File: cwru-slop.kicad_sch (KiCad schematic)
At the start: 65 parts, among them J1 USB_C_Receptacle_USB2.0_16P, J2 FTSH-105-01-L-DV-007-K, J3 Conn_01x03_Pin, J4 54-00320, U1 TLV9001IDCK, U10 B3U-1000P, U11 TLV9001IDCK, U12 TLV9001IDCK, U2 AP63205WU, U3 TLV75533PDBV, U4 STM32L433CCTx, U5 TPS2116DRL, U6 FXLS8974CFR3, U7 ESDCAN24-2BLY, U8 MCP2562-E-SN, U9 24lc32at-i/ot, Y1 XRCGB24M000F3M00R0

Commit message: erc, remove vdda filtering (check if nec), clean
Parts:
- removed C6: 10n, Capacitor_SMD:C_0603_1608Metric_Pad1.08x0.95mm_HandSolder, symbol slopp:C
- removed C7, C8: 1u, Capacitor_SMD:C_0603_1608Metric_Pad1.08x0.95mm_HandSolder, symbol slopp:C
- removed FB1: 120R, Package_QFP:LQFP-48_7x7mm_P0.5mm, symbol Device:FerriteBead
- C14: value 1u -> 10u
- C3: value 100n -> 10n
- C4: value 100n -> 1u
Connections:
- net +3.3V is gone; now on net +3V3: C1.1, C2.1, C3.1, C4.1, C5.1, U4.1 (VBAT), U4.24 (VDD), U4.36 (VDDUSB), U4.48 (VDD)
- net +3.3VA is gone; now on net +3V3: U4.9 (VDDA)
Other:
- moved on the sheet: C1, C2, C3, C4, C5

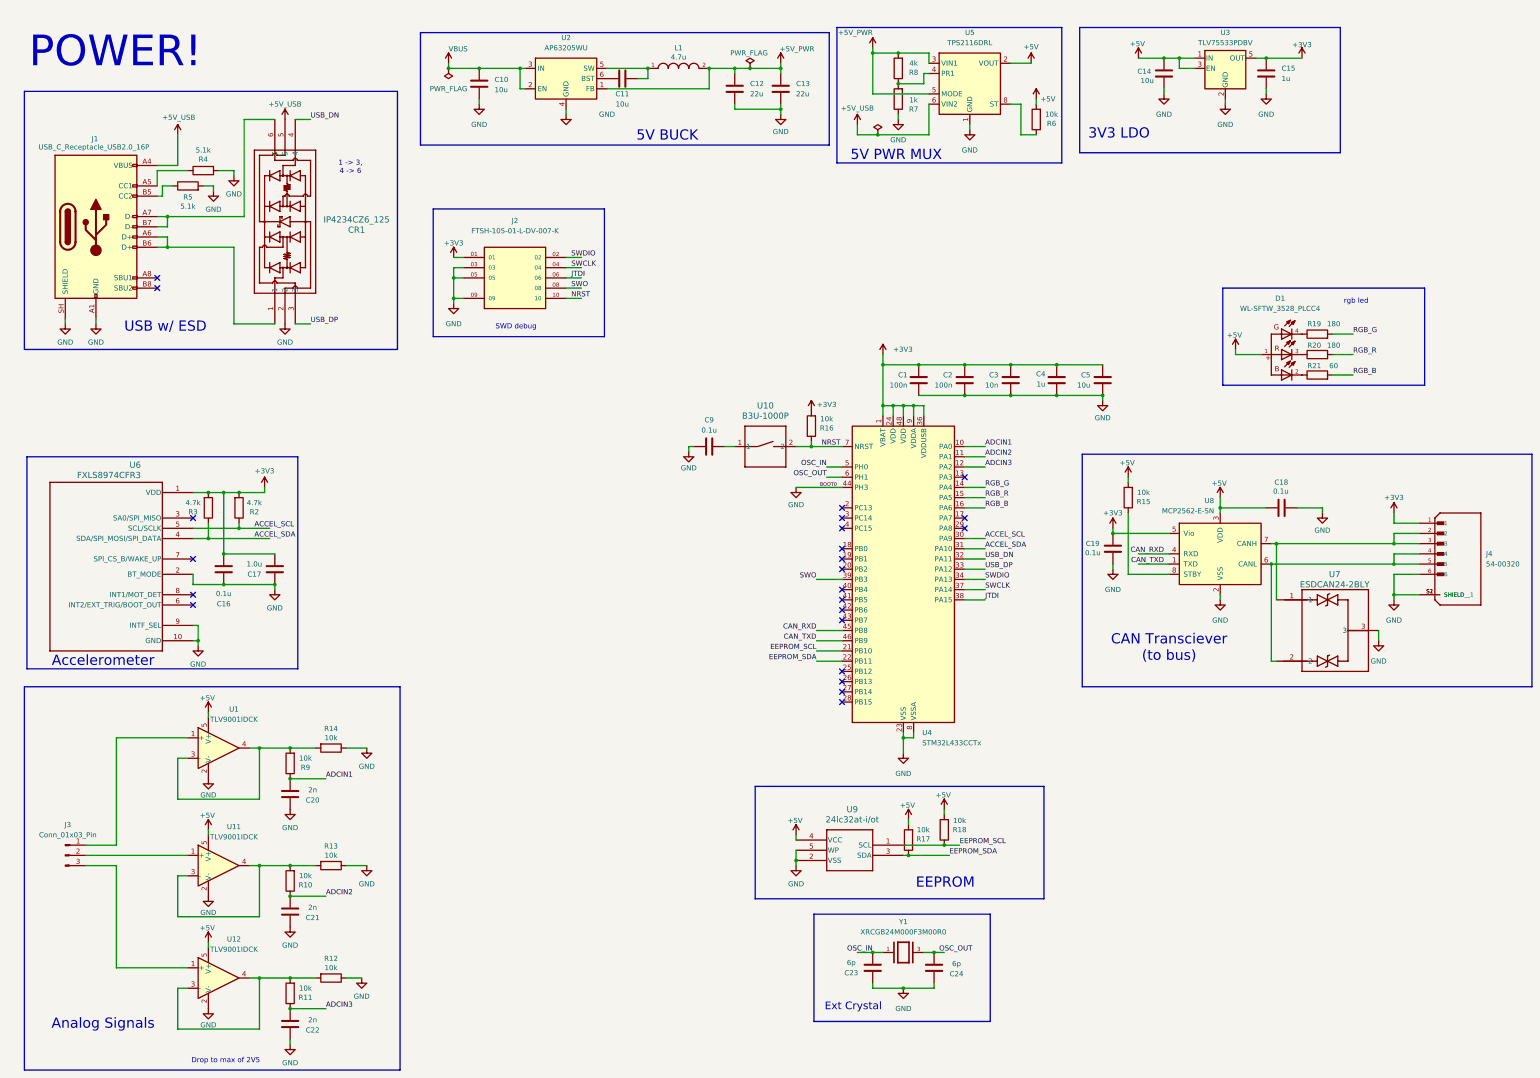
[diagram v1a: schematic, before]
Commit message: tie accel bt_mode to gnd
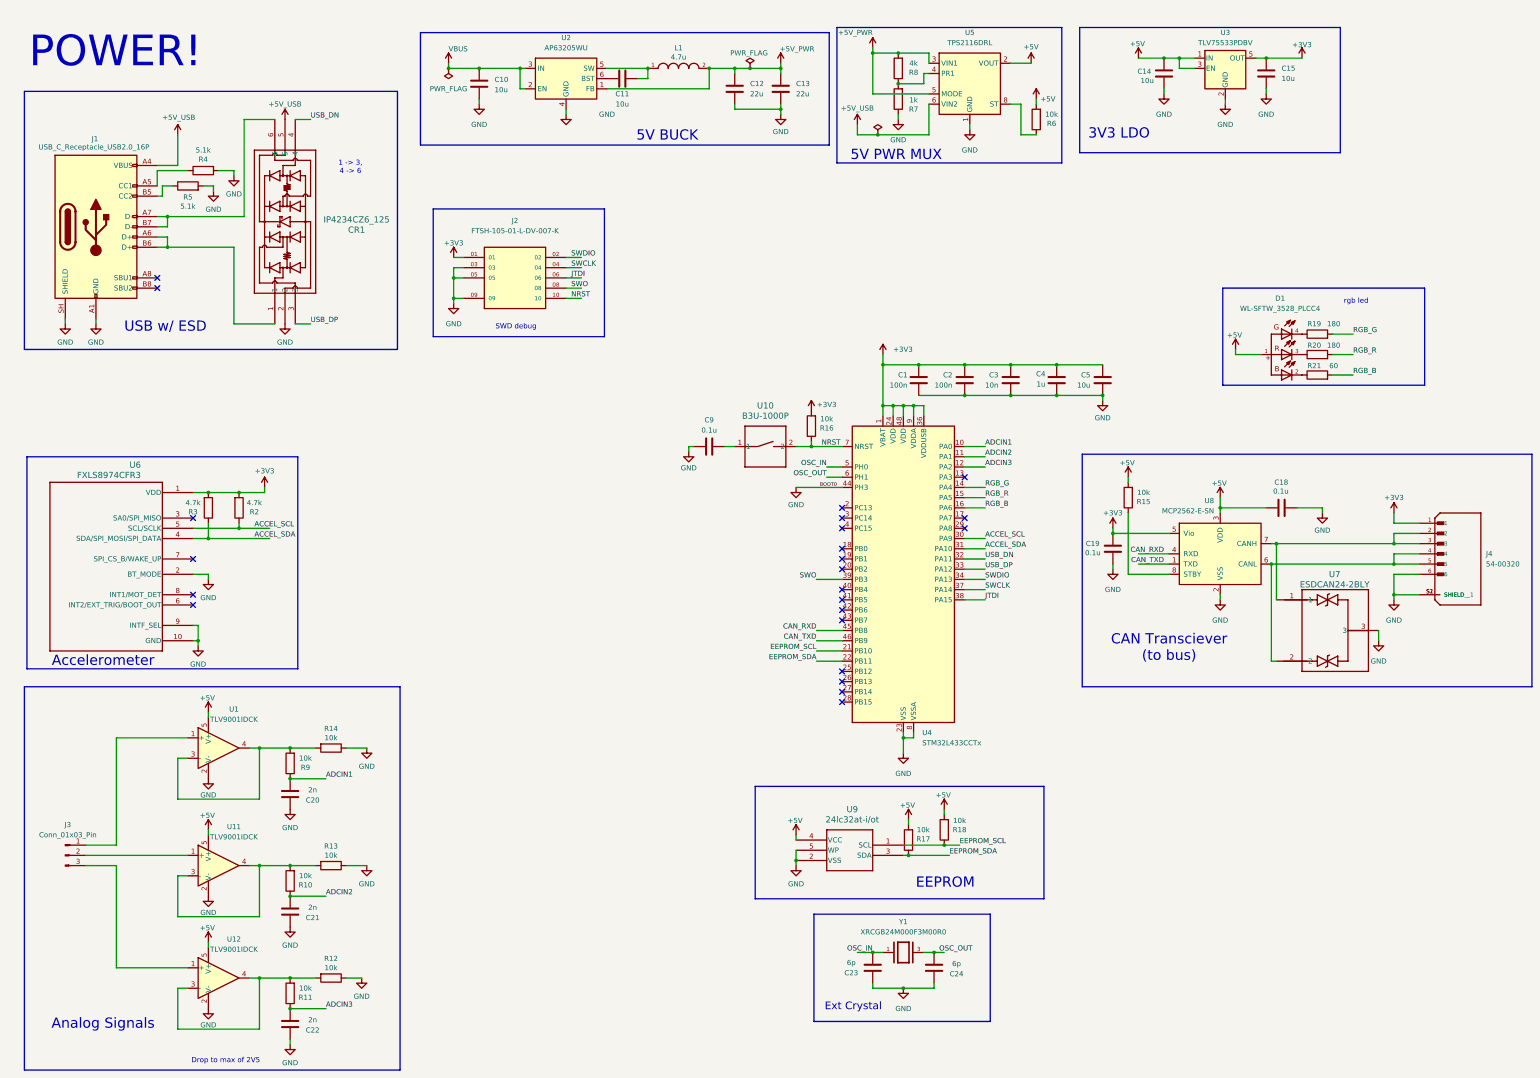
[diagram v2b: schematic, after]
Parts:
- removed C16: 0.1u, Capacitor_SMD:C_0603_1608Metric_Pad1.08x0.95mm_HandSolder, symbol slopp:C
- removed C17: 1.0u, Capacitor_SMD:C_0603_1608Metric_Pad1.08x0.95mm_HandSolder, symbol slopp:C
- C15: value 1u -> 10u
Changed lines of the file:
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@@
 	)
 	(junction
-		(at 85.09 157.48)
-		(diameter 0)
-		(color 0 0 0 0)
-	)
-	(junction
 		(at 332.74 152.4)
 		(diameter 0)
@@
 	)
 	(junction
-		(at 72.39 134.62)
-		(diameter 0)
-		(color 0 0 0 0)
-	)
-	(junction
 		(at 214.63 226.06)
 		(diameter 0)
@@
 	)
 	(junction
-		(at 72.39 157.48)
-		(diameter 0)
-		(color 0 0 0 0)
-	)
-	(junction
 		(at 293.37 144.78)
 		(diameter 0)
@@
 	)
 	(junction
-		(at 72.39 149.86)
-		(diameter 0)
-		(color 0 0 0 0)
-	)
-	(junction
 		(at 218.44 123.19)
 		(diameter 0)
@@
 	(wire
 		(pts
-			(xy 72.39 149.86) (xy 85.09 149.86)
-		)
-		(stroke
-			(width 0)
-			(type default)
-		)
-	)
-	(wire
-		(pts
 			(xy 68.58 189.23) (xy 68.58 190.5)
 		)
@@
 	(wire
 		(pts
-			(xy 72.39 157.48) (xy 64.77 157.48)
-		)
-		(stroke
-			(width 0)
-			(type default)
-		)
-	)
-	(wire
-		(pts
 			(xy 363.22 154.94) (xy 363.22 161.29)
 		)
@@
 	(wire
 		(pts
-			(xy 85.09 158.75) (xy 85.09 157.48)
-		)
-		(stroke
-			(width 0)
-			(type default)
-		)
-	)
-	(wire
-		(pts
 			(xy 177.8 29.21) (xy 177.8 31.75)
 		)
@@
 	(wire
 		(pts
-			(xy 82.55 134.62) (xy 64.77 134.62)
+			(xy 64.77 134.62) (xy 82.55 134.62)
 		)
 		(stroke
@@
 	(wire
 		(pts
-			(xy 72.39 134.62) (xy 72.39 149.86)
-		)
-		(stroke
-			(width 0)
-			(type default)
-		)
-	)
-	(wire
-		(pts
 			(xy 60.96 267.97) (xy 81.28 267.97)
 		)
@@
 	(wire
 		(pts
+			(xy 68.58 154.94) (xy 64.77 154.94)
+		)
+		(stroke
+			(width 0)
+			(type default)
+		)
+	)
+	(wire
+		(pts
 			(xy 81.28 255.27) (xy 88.9 255.27)
 		)
@@
 	(wire
 		(pts
-			(xy 85.09 157.48) (xy 72.39 157.48)
-		)
-		(stroke
-			(width 0)
-			(type default)
-		)
-	)
-	(wire
-		(pts
 			(xy 74.93 92.71) (xy 85.09 92.71)
 		)
@@
 	(wire
 		(pts
-			(xy 64.77 157.48) (xy 64.77 154.94)
+			(xy 68.58 156.21) (xy 68.58 154.94)
 		)
 		(stroke
@@
 	(symbol
 		(lib_id "power:GND")
+		(at 68.58 156.21 0)
+		(mirror y)
+		(unit 1)
+		(body_style 1)
+		(exclude_from_sim no)
+		(in_bom yes)
+		(on_board yes)
+		(in_pos_files yes)
+		(dnp no)
+		(property "Reference" "#PWR066"
+			(at 68.58 162.56 0)
+			(hide yes)
+			(show_name no)
+			(do_not_autoplace no)
+			(effects
+				(font
+					(size 1.27 1.27)
+				)
+			)
+		)
+		(property "Value" "GND"
+			(at 68.58 160.782 0)
+			(show_name no)
+			(do_not_autoplace no)
+			(effects
+				(font
+					(size 1.27 1.27)
+				)
+			)
+		)
+		(property "Footprint" ""
+			(at 68.58 156.21 0)
+			(hide yes)
+			(show_name no)
+			(do_not_autoplace no)
+			(effects
+				(font
+					(size 1.27 1.27)
+				)
+			)
+		)
+		(property "Datasheet" ""
+			(at 68.58 156.21 0)
+			(hide yes)
+			(show_name no)
+			(do_not_autoplace no)
+			(effects
+				(font
+					(size 1.27 1.27)
+				)
+			)
+		)
+		(property "Description" "Power symbol creates a global label with name \"GND\" , ground"
+			(at 68.58 156.21 0)
+			(hide yes)
+			(show_name no)
+			(do_not_autoplace no)
+			(effects
+				(font
+					(size 1.27 1.27)
+				)
+			)
+		)
+		(pin "1"
+		)
+		(instances
+			(project "cwru-slop"
+				(path "/e1282a69-b748-44db-b34f-024ba2d0c37d"
+					(reference "#PWR066")
+					(unit 1)
+				)
+			)
+		)
+	)
+	(symbol
+		(lib_id "power:GND")
 		(at 293.37 153.67 0)
 		(unit 1)
@@
 	)
 	(symbol
-		(lib_id "slopp:C")
-		(at 72.39 153.67 0)
-		(mirror x)
-		(unit 1)
-		(body_style 1)
-		(exclude_from_sim no)
-		(in_bom yes)
-		(on_board yes)
-		(in_pos_files yes)
-		(dnp no)
-		(property "Reference" "C16"
-			(at 72.39 162.306 0)
-			(show_name no)
-			(do_not_autoplace no)
-			(effects
-				(font
-					(size 1.27 1.27)
-				)
-			)
-		)
-		(property "Value" "0.1u"
-			(at 72.39 159.766 0)
-			(show_name no)
-			(do_not_autoplace no)
-			(effects
-				(font
-					(size 1.27 1.27)
-				)
-			)
-		)
-		(property "Footprint" "Capacitor_SMD:C_0603_1608Metric_Pad1.08x0.95mm_HandSolder"
-			(at 73.3552 149.86 0)
-			(hide yes)
-			(show_name no)
-			(do_not_autoplace no)
-			(effects
-				(font
-					(size 1.27 1.27)
-				)
-			)
-		)
-		(property "Datasheet" ""
-			(at 72.39 153.67 0)
-			(hide yes)
-			(show_name no)
-			(do_not_autoplace no)
-			(effects
-				(font
-					(size 1.27 1.27)
-				)
-			)
-		)
-		(property "Description" "Unpolarized capacitor"
-			(at 72.39 153.67 0)
-			(hide yes)
-			(show_name no)
-			(do_not_autoplace no)
-			(effects
-				(font
-					(size 1.27 1.27)
-				)
-			)
-		)
-		(pin "2"
-		)
-		(pin "1"
-		)
-		(instances
-			(project "cwru-slop"
-				(path "/e1282a69-b748-44db-b34f-024ba2d0c37d"
-					(reference "C16")
-					(unit 1)
-				)
-			)
-		)
-	)
-	(symbol
 		(lib_id "power:GND")
 		(at 345.44 139.7 0)
@@
 	)
 	(symbol
-		(lib_id "power:GND")
-		(at 85.09 158.75 0)
-		(mirror y)
-		(unit 1)
-		(body_style 1)
-		(exclude_from_sim no)
-		(in_bom yes)
-		(on_board yes)
-		(in_pos_files yes)
-		(dnp no)
-		(property "Reference" "#PWR026"
-			(at 85.09 165.1 0)
-			(hide yes)
-			(show_name no)
-			(do_not_autoplace no)
-			(effects
-				(font
-					(size 1.27 1.27)
-				)
-			)
-		)
-		(property "Value" "GND"
-			(at 85.09 163.322 0)
-			(show_name no)
-			(do_not_autoplace no)
-			(effects
-				(font
-					(size 1.27 1.27)
-				)
-			)
-		)
-		(property "Footprint" ""
-			(at 85.09 158.75 0)
-			(hide yes)
-			(show_name no)
-			(do_not_autoplace no)
-			(effects
-				(font
-					(size 1.27 1.27)
-				)
-			)
-		)
-		(property "Datasheet" ""
-			(at 85.09 158.75 0)
-			(hide yes)
-			(show_name no)
-			(do_not_autoplace no)
-			(effects
-				(font
-					(size 1.27 1.27)
-				)
-			)
-		)
-		(property "Description" "Power symbol creates a global label with name \"GND\" , ground"
-			(at 85.09 158.75 0)
-			(hide yes)
-			(show_name no)
-			(do_not_autoplace no)
-			(effects
-				(font
-					(size 1.27 1.27)
-				)
-			)
-		)
-		(pin "1"
-		)
-		(instances
-			(project "cwru-slop"
-				(path "/e1282a69-b748-44db-b34f-024ba2d0c37d"
-					(reference "#PWR026")
-					(unit 1)
-				)
-			)
-		)
-	)
-	(symbol
 		(lib_id "power:+5V")
 		(at 297.18 130.81 0)
@@
 			)
 		)
-		(property "Value" "1u"
+		(property "Value" "10u"
 			(at 335.28 31.75 0)
 			(show_name no)
@@
 					(unit 1)
 				)
-			)
-		)
-	)
-	(symbol
-		(lib_id "slopp:C")
-		(at 85.09 153.67 0)
-		(mirror x)
-		(unit 1)
-		(body_style 1)
-		(exclude_from_sim no)
-		(in_bom yes)
-		(on_board yes)
-		(in_pos_files yes)
-		(dnp no)
-		(property "Reference" "C17"
-			(at 80.01 154.94 0)
-			(show_name no)
-			(do_not_autoplace no)
-			(effects
-				(font
-					(size 1.27 1.27)
-				)
-			)
-		)
-		(property "Value" "1.0u"
-			(at 80.01 152.4 0)
-			(show_name no)
-			(do_not_autoplace no)
-			(effects
-				(font
-					(size 1.27 1.27)
-				)
-			)
-		)
-		(property "Footprint" "Capacitor_SMD:C_0603_1608Metric_Pad1.08x0.95mm_HandSolder"
-			(at 86.0552 149.86 0)
-			(hide yes)
-			(show_name no)
-			(do_not_autoplace no)
-			(effects
-				(font
-					(size 1.27 1.27)
-				)
-			)
-		)
-		(property "Datasheet" ""
-			(at 85.09 153.67 0)
-			(hide yes)
-			(show_name no)
-			(do_not_autoplace no)
-			(effects
-				(font
-					(size 1.27 1.27)
-				)
-			)
-		)
-		(property "Description" "Unpolarized capacitor"
-			(at 85.09 153.67 0)
-			(hide yes)
-			(show_name no)
-			(do_not_autoplace no)
-			(effects
-				(font
-					(size 1.27 1.27)
-				)
-			)
-		)
-		(pin "2"
-		)
-		(pin "1"
-		)
-		(instances
-			(project "cwru-slop"
-				(path "/e1282a69-b748-44db-b34f-024ba2d0c37d"
-					(reference "C17")
-					(unit 1)
-				)

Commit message: led resistor vals
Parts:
- R19: value 180 -> 90
- R20: value 180 -> 150
- R21: value 60 -> 90
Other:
- note added: "rgb led (20mA)"
- note removed: "rgb led"
- moved on the sheet: C10, C11, C12, C13, C14, C15, C20, C21, C22, C23, C24, CR1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

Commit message: remove jtdi conn
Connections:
- net SWO: now also J2.06; no longer J2.08
- net JTDI: no longer names the net of U4.38 (PA15)
- net JTDI: no longer J2.06
- no-connect marks 23 -> 25
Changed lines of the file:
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@@
+	)
+	(no_connect
+		(at 256.54 161.29)
 	)
 	(no_connect
@@
 	)
 	(no_connect
+		(at 177.8 153.67)
+	)
+	(no_connect
 		(at 113.03 138.43)
 	)
@@
 	(wire
 		(pts
-			(xy 177.8 153.67) (xy 181.61 153.67)
-		)
-		(stroke
-			(width 0)
-			(type default)
-		)
-	)
-	(wire
-		(pts
 			(xy 334.01 147.32) (xy 334.01 161.29)
 		)
@@
 		(pts
 			(xy 339.09 138.43) (xy 345.44 138.43)
-		)
-		(stroke
-			(width 0)
-			(type default)
-		)
-	)
-	(wire
-		(pts
-			(xy 256.54 161.29) (xy 261.62 161.29)
 		)
 		(stroke
@@
 		)
 	)
-	(label "JTDI"
-		(at 261.62 161.29 0)
-		(effects
-			(font
-				(size 1.27 1.27)
-			)
-			(justify left bottom)
-		)
-	)
 	(label "EEPROM_SCL"
 		(at 219.71 173.99 180)
@@
 	)
 	(label "SWO"
-		(at 179.07 153.67 0)
+		(at 179.07 151.13 0)
 		(effects
 			(font
@@
 		(effects
 			(font
-				(size 1.27 1.27)
-			)
-			(justify left bottom)
-		)
-	)
-	(label "JTDI"
-		(at 179.07 151.13 0)
-		(effects
-			(font

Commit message: start pcb, add necessary footprints, update lowpass caps and i forgot
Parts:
- added C6: 4.7u, Capacitor_SMD:C_0603_1608Metric_Pad1.08x0.95mm_HandSolder, symbol slopp:C
- C20, C21, C22: value 2n -> 20n
- J4: footprint 54-00320:TENSILITY_54-00320 -> SYS27_Footprints:TENSILITY_54-00320
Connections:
- net +3V3: now also C6.1
- net GND: now also C6.2
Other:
- moved on the sheet: C4, C5
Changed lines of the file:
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@@
 	(text "POWER!"
 		(exclude_from_sim no)
-		(at 45.466 25.146 0)
+		(at 137.922 22.352 0)
 		(effects
 			(font
@@
 	)
 	(junction
+		(at 299.72 110.49)
+		(diameter 0)
+		(color 0 0 0 0)
+	)
+	(junction
 		(at 214.63 35.56)
 		(diameter 0)
@@
 	)
 	(junction
-		(at 279.4 110.49)
+		(at 278.13 110.49)
 		(diameter 0)
 		(color 0 0 0 0)
@@
 	)
 	(junction
-		(at 279.4 102.87)
+		(at 278.13 102.87)
 		(diameter 0)
 		(color 0 0 0 0)
@@
 	)
 	(junction
-		(at 290.83 110.49)
+		(at 288.29 110.49)
 		(diameter 0)
 		(color 0 0 0 0)
@@
 	)
 	(junction
+		(at 288.29 102.87)
+		(diameter 0)
+		(color 0 0 0 0)
+	)
+	(junction
 		(at 284.48 69.85)
 		(diameter 0)
@@
 	(wire
 		(pts
-			(xy 236.22 102.87) (xy 290.83 102.87)
+			(xy 236.22 102.87) (xy 299.72 102.87)
 		)
 		(stroke
@@
 	(wire
 		(pts
-			(xy 267.97 110.49) (xy 279.4 110.49)
+			(xy 267.97 110.49) (xy 299.72 110.49)
 		)
 		(stroke
@@
 	(wire
 		(pts
-			(xy 279.4 110.49) (xy 290.83 110.49)
-		)
-		(stroke
-			(width 0)
-			(type default)
-		)
-	)
-	(wire
-		(pts
 			(xy 256.54 153.67) (xy 261.62 153.67)
 		)
@@
 	(wire
 		(pts
-			(xy 290.83 111.76) (xy 290.83 110.49)
+			(xy 299.72 111.76) (xy 299.72 110.49)
 		)
 		(stroke
@@
 			)
 		)
-		(property "Value" "2n"
+		(property "Value" "20n"
 			(at 142.748 252.984 0)
 			(show_name no)
@@
 	(symbol
 		(lib_id "slopp:C")
-		(at 290.83 106.68 0)
+		(at 288.29 106.68 0)
 		(mirror y)
 		(unit 1)
@@
 		(dnp no)
 		(property "Reference" "C5"
-			(at 287.782 105.41 0)
+			(at 285.242 105.41 0)
 			(show_name no)
 			(do_not_autoplace no)
@@
 		)
 		(property "Value" "10u"
-			(at 287.782 107.95 0)
+			(at 285.242 107.95 0)
 			(show_name no)
 			(do_not_autoplace no)
@@
 		)
 		(property "Footprint" "Capacitor_SMD:C_0603_1608Metric_Pad1.08x0.95mm_HandSolder"
-			(at 289.8648 110.49 0)
+			(at 287.3248 110.49 0)
 			(hide yes)
 			(show_name no)
@@
 		)
 		(property "Datasheet" ""
-			(at 290.83 106.68 0)
+			(at 288.29 106.68 0)
 			(hide yes)
 			(show_name no)
@@
 		)
 		(property "Description" "Unpolarized capacitor"
-			(at 290.83 106.68 0)
+			(at 288.29 106.68 0)
 			(hide yes)
 			(show_name no)
@@
 			)
 		)
-		(property "Value" "2n"
+		(property "Value" "20n"
 			(at 142.748 225.044 0)
 			(show_name no)
@@
 	)
 	(symbol
+		(lib_id "slopp:C")
+		(at 299.72 106.68 0)
+		(mirror y)
+		(unit 1)
+		(body_style 1)
+		(exclude_from_sim no)
+		(in_bom yes)
+		(on_board yes)
+		(in_pos_files yes)
+		(dnp no)
+		(property "Reference" "C6"
+			(at 296.926 105.156 0)
+			(show_name no)
+			(do_not_autoplace no)
+			(effects
+				(font
+					(size 1.27 1.27)
+				)
+				(justify left)
+			)
+		)
+		(property "Value" "4.7u"
+			(at 296.926 107.696 0)
+			(show_name no)
+			(do_not_autoplace no)
+			(effects
+				(font
+					(size 1.27 1.27)
+				)
+				(justify left)
+			)
+		)
+		(property "Footprint" "Capacitor_SMD:C_0603_1608Metric_Pad1.08x0.95mm_HandSolder"
+			(at 298.7548 110.49 0)
+			(hide yes)
+			(show_name no)
+			(do_not_autoplace no)
+			(effects
+				(font
+					(size 1.27 1.27)
+				)
+			)
+		)
+		(property "Datasheet" ""
+			(at 299.72 106.68 0)
+			(hide yes)
+			(show_name no)
+			(do_not_autoplace no)
+			(effects
+				(font
+					(size 1.27 1.27)
+				)
+			)
+		)
+		(property "Description" "Unpolarized capacitor"
+			(at 299.72 106.68 0)
+			(hide yes)
+			(show_name no)
+			(do_not_autoplace no)
+			(effects
+				(font
+					(size 1.27 1.27)
+				)
+			)
+		)
+		(pin "2"
+		)
+		(pin "1"
+		)
+		(instances
+			(project "cwru-slop"
+				(path "/e1282a69-b748-44db-b34f-024ba2d0c37d"
+					(reference "C6")
+					(unit 1)
+				)
+			)
+		)
+	)
+	(symbol
 		(lib_id "power:GND")
 		(at 222.25 228.6 0)
@@
 			)
 		)
-		(property "Footprint" "54-00320:TENSILITY_54-00320"
+		(property "Footprint" "SYS27_Footprints:TENSILITY_54-00320"
 			(at 379.73 149.86 0)
 			(hide yes)
@@
 	(symbol
 		(lib_id "slopp:C")
-		(at 279.4 106.68 0)
+		(at 278.13 106.68 0)
 		(mirror y)
 		(unit 1)
@@
 		(dnp no)
 		(property "Reference" "C4"
-			(at 276.606 105.156 0)
+			(at 275.336 105.156 0)
 			(show_name no)
 			(do_not_autoplace no)
@@
 		)
 		(property "Value" "1u"
-			(at 276.606 107.696 0)
+			(at 275.336 107.696 0)
 			(show_name no)
 			(do_not_autoplace no)
@@
 		)
 		(property "Footprint" "Capacitor_SMD:C_0603_1608Metric_Pad1.08x0.95mm_HandSolder"
-			(at 278.4348 110.49 0)
+			(at 277.1648 110.49 0)
 			(hide yes)
 			(show_name no)
@@
 		)
 		(property "Datasheet" ""
-			(at 279.4 106.68 0)
+			(at 278.13 106.68 0)
 			(hide yes)
 			(show_name no)
@@
 		)
 		(property "Description" "Unpolarized capacitor"
-			(at 279.4 106.68 0)
+			(at 278.13 106.68 0)
 			(hide yes)
 			(show_name no)
@@
 			)
 		)
-		(property "Value" "2n"
+		(property "Value" "20n"
 			(at 142.748 195.834 0)
 			(show_name no)
@@
 	(symbol
 		(lib_id "power:GND")
-		(at 290.83 111.76 0)
+		(at 299.72 111.76 0)
 		(mirror y)
 		(unit 1)
@@
 		(dnp no)
 		(property "Reference" "#PWR04"
-			(at 290.83 118.11 0)
+			(at 299.72 118.11 0)
 			(hide yes)
 			(show_name no)
@@
 		)
 		(property "Value" "GND"
-			(at 290.83 116.078 0)
+			(at 299.72 116.078 0)
 			(show_name no)
 			(do_not_autoplace no)
@@
 		)
 		(property "Footprint" ""
-			(at 290.83 111.76 0)
+			(at 299.72 111.76 0)
 			(hide yes)
 			(show_name no)
@@
 		)
 		(property "Datasheet" ""
-			(at 290.83 111.76 0)
+			(at 299.72 111.76 0)
 			(hide yes)
 			(show_name no)
@@
 		)
 		(property "Description" "Power symbol creates a global label with name \"GND\" , ground"
-			(at 290.83 111.76 0)
+			(at 299.72 111.76 0)
 			(hide yes)
 			(show_name no)

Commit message: idk what was unsaved
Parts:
- J1: footprint SYS27_Footprints:B3U-1000P -> Connector_USB:USB_C_Receptacle_GCT_USB4105-xx-A_16P_TopMnt_Horizontal
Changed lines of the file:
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@@
 			)
 		)
-		(property "Footprint" "SYS27_Footprints:B3U-1000P"
+		(property "Footprint" "Connector_USB:USB_C_Receptacle_GCT_USB4105-xx-A_16P_TopMnt_Horizontal"
 			(at 110.49 63.5 0)
 			(hide yes)
